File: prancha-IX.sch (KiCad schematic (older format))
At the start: 32 parts

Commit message: conector de 70 pinos para a interconexão das placas e término do desenho da prancha 5.
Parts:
- added P?: CONN_35X2, symbol CONN_35X2
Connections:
- new net ?: P?.1 (P1), P?.10 (P10), P?.11 (P11), P?.12 (P12), P?.13 (P13), P?.14 (P14), P?.15 (P15), P?.16 (P16), P?.17 (P17), P?.18 (P18), P?.19 (P19), P?.2 (P2), P?.20 (P20), P?.21 (P21), P?.22 (P22), P?.23 (P23), P?.24 (P24), P?.25, P?.26 (P26), P?.27 (P27), P?.28 (P28), P?.29 (P29), P?.3 (P3), P?.30 (P30), P?.31 (P31), P?.32 (P32), P?.33 (P33), P?.34 (P34), P?.35 (P35), P?.36 (P36), P?.37 (P37), P?.38 (P38), P?.39 (P39), P?.4 (P4), P?.40 (P40), P?.41 (P41), P?.42 (P42), P?.43 (P43), P?.44 (P44), P?.45 (P45), P?.46 (P46), P?.47 (P47), P?.48 (P48), P?.49 (P49), P?.5 (P5), P?.50 (P50), P?.51 (P51), P?.52 (P52), P?.53 (P53), P?.54 (P54), P?.55 (P55), P?.56 (P56), P?.57 (P57), P?.58 (P58), P?.59 (P59), P?.6 (P6), P?.60 (P60), P?.61 (P61), P?.62 (P62), P?.63 (P63), P?.64 (P64), P?.65 (P65), P?.66 (P66), P?.67 (P67), P?.68 (P68), P?.69 (P69), P?.7 (P7), P?.70 (P70), P?.8 (P8), P?.9 (P9)
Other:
- moved on the sheet: 1A_P9A, 1A_P9B, 1B_P9A, 1B_P9B, 1C_P9A, 1C_P9B, 1D_P9A, 1D_P9B, 1E_P9A, 1E_P9B, 1E_P9C, 1E_P9D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

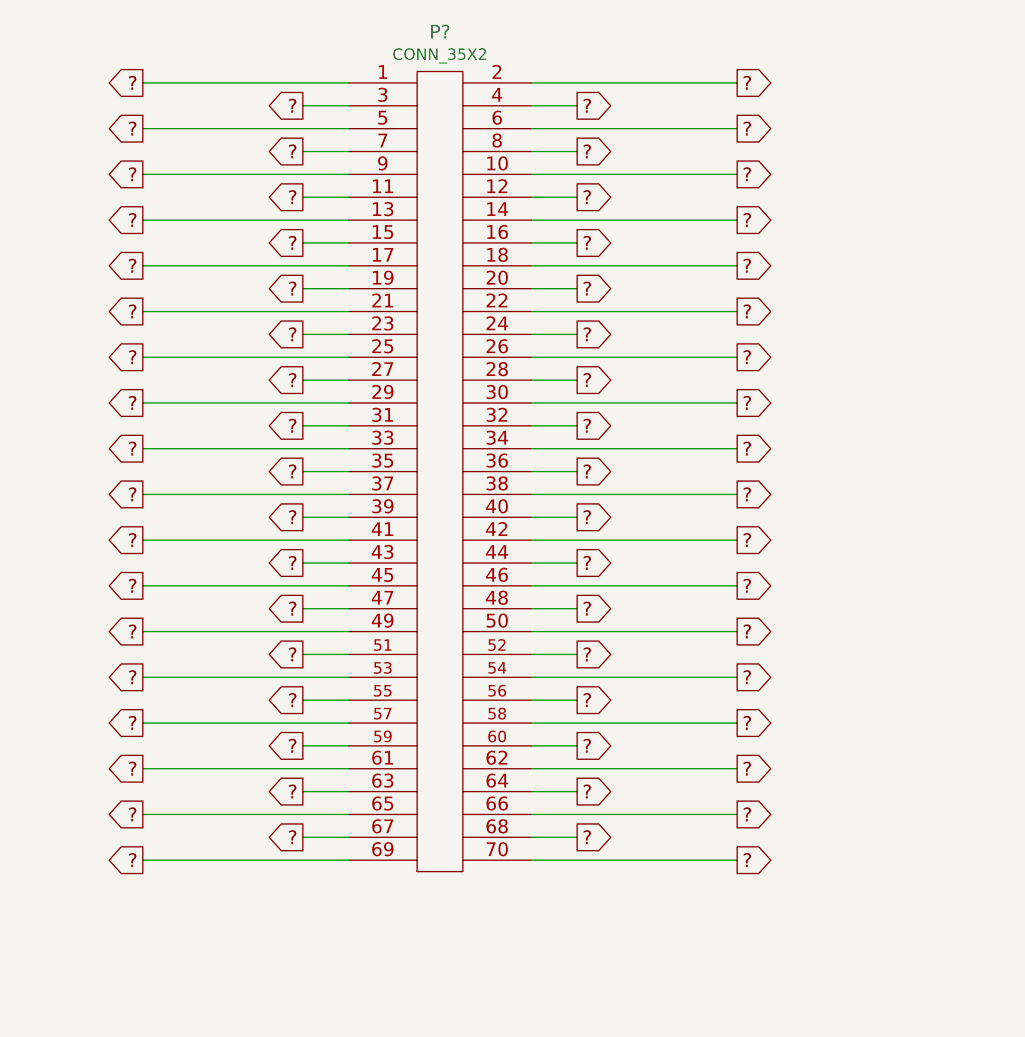
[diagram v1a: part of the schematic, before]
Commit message: sinais do conector da prancha 9
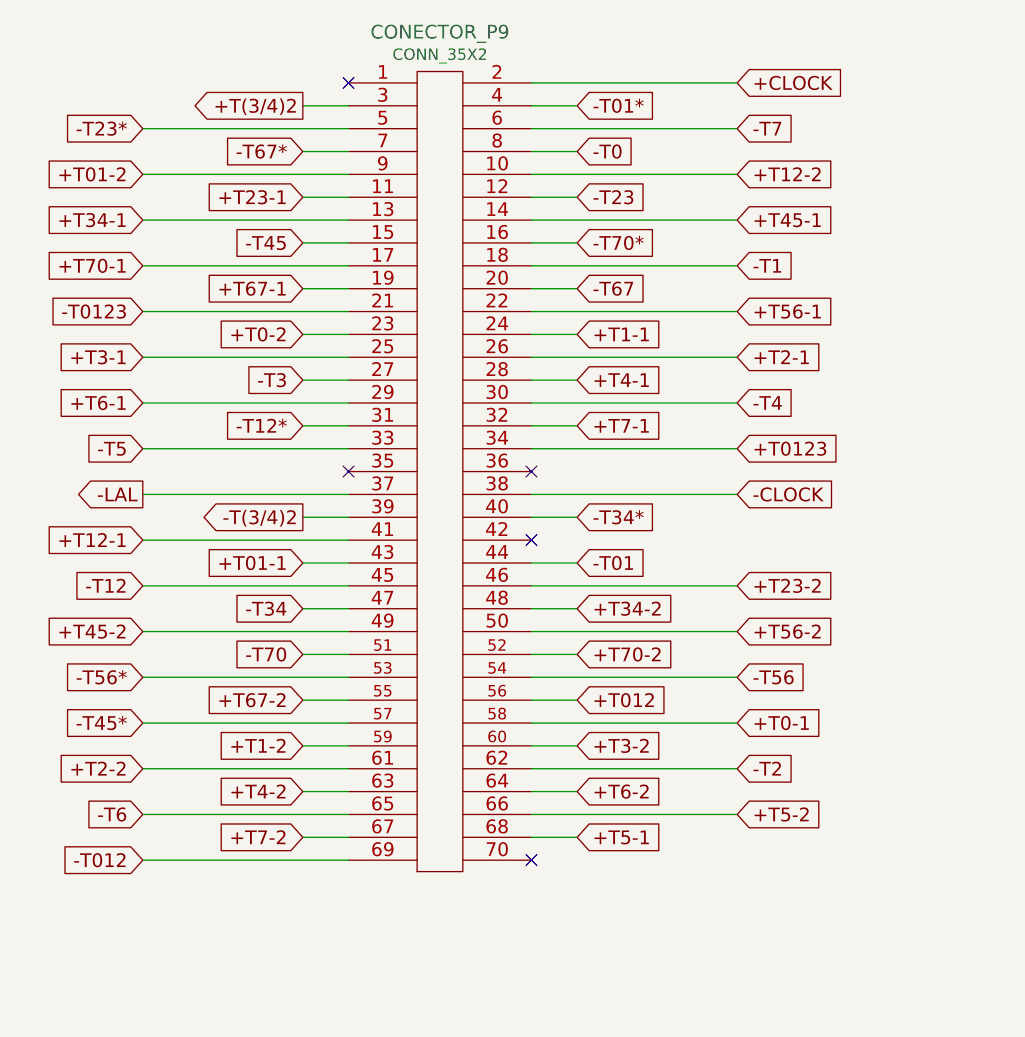
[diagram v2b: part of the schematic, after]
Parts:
- gave numbers to parts that had none: 1
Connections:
- net +CLOCK: now also CONECTOR_P9.2 (P2)
- net +T(3/4)2: now also CONECTOR_P9.3 (P3)
- net +T0-1: now also CONECTOR_P9.58 (P58)
- net +T0-2: now also CONECTOR_P9.23 (P23)
- net +T01-1: now also CONECTOR_P9.43 (P43)
- net +T01-2: now also CONECTOR_P9.9 (P9)
- net +T012: now also CONECTOR_P9.56 (P56)
- net +T0123: now also CONECTOR_P9.34 (P34)
- net +T1-1: now also CONECTOR_P9.24 (P24)
- net +T1-2: now also CONECTOR_P9.59 (P59)
- net +T12-1: now also CONECTOR_P9.41 (P41)
- net +T12-2: now also CONECTOR_P9.10 (P10)
- net +T2-1: now also CONECTOR_P9.26 (P26)
- net +T2-2: now also CONECTOR_P9.61 (P61)
- net +T23-1: now also CONECTOR_P9.11 (P11)
- net +T23-2: now also CONECTOR_P9.46 (P46)
- net +T3-1: now also CONECTOR_P9.25
- net +T3-2: now also CONECTOR_P9.60 (P60)
- net +T34-1: now also CONECTOR_P9.13 (P13)
- net +T34-2: now also CONECTOR_P9.48 (P48)
- net +T4-1: now also CONECTOR_P9.28 (P28)
- net +T4-2: now also CONECTOR_P9.63 (P63)
- net +T45-1: now also CONECTOR_P9.14 (P14)
- net +T45-2: now also CONECTOR_P9.49 (P49)
- net +T5-1: now also CONECTOR_P9.68 (P68)
- net +T5-2: now also CONECTOR_P9.66 (P66)
- net +T56-1: now also CONECTOR_P9.22 (P22)
- net +T56-2: now also CONECTOR_P9.50 (P50)
- net +T6-1: now also CONECTOR_P9.29 (P29)
- net +T6-2: now also CONECTOR_P9.64 (P64)
- net +T67-1: now also CONECTOR_P9.19 (P19)
- net +T67-2: now also CONECTOR_P9.55 (P55)
- net +T7-1: now also CONECTOR_P9.32 (P32)
- net +T7-2: now also CONECTOR_P9.67 (P67)
- net +T70-1: now also CONECTOR_P9.17 (P17)
- net +T70-2: now also CONECTOR_P9.52 (P52)
- net -CLOCK: now also CONECTOR_P9.38 (P38)
- net -LAL: now also CONECTOR_P9.37 (P37)
- net -T(3/4)2: now also CONECTOR_P9.39 (P39)
- net -T0: now also CONECTOR_P9.8 (P8)
- net -T01: now also CONECTOR_P9.44 (P44)
- net -T01*: now also CONECTOR_P9.4 (P4)
- net -T012: now also CONECTOR_P9.69 (P69)
- net -T0123: now also CONECTOR_P9.21 (P21)
- net -T1: now also CONECTOR_P9.18 (P18)
- net -T12: now also CONECTOR_P9.45 (P45)
- net -T12*: now also CONECTOR_P9.31 (P31)
- net -T2: now also CONECTOR_P9.62 (P62)
- net -T23: now also CONECTOR_P9.12 (P12)
- net -T23*: now also CONECTOR_P9.5 (P5)
- net -T3: now also CONECTOR_P9.27 (P27)
- net -T34: now also CONECTOR_P9.47 (P47)
- net -T34*: now also CONECTOR_P9.40 (P40)
- net -T4: now also CONECTOR_P9.30 (P30)
- net -T45: now also CONECTOR_P9.15 (P15)
- net -T45*: now also CONECTOR_P9.57 (P57)
- net -T5: now also CONECTOR_P9.33 (P33)
- net -T56: now also CONECTOR_P9.54 (P54)
- net -T56*: now also CONECTOR_P9.53 (P53)
- net -T6: now also CONECTOR_P9.65 (P65)
- net -T67: now also CONECTOR_P9.20 (P20)
- net -T67*: now also CONECTOR_P9.7 (P7)
- net -T7: now also CONECTOR_P9.6 (P6)
- net -T70: now also CONECTOR_P9.51 (P51)
- net -T70*: now also CONECTOR_P9.16 (P16)
- removed net ?: CONECTOR_P9.1 (P1), CONECTOR_P9.10 (P10), CONECTOR_P9.11 (P11), CONECTOR_P9.12 (P12), CONECTOR_P9.13 (P13), CONECTOR_P9.14 (P14), CONECTOR_P9.15 (P15), CONECTOR_P9.16 (P16), CONECTOR_P9.17 (P17), CONECTOR_P9.18 (P18), CONECTOR_P9.19 (P19), CONECTOR_P9.2 (P2), CONECTOR_P9.20 (P20), CONECTOR_P9.21 (P21), CONECTOR_P9.22 (P22), CONECTOR_P9.23 (P23), CONECTOR_P9.24 (P24), CONECTOR_P9.25, CONECTOR_P9.26 (P26), CONECTOR_P9.27 (P27), CONECTOR_P9.28 (P28), CONECTOR_P9.29 (P29), CONECTOR_P9.3 (P3), CONECTOR_P9.30 (P30), CONECTOR_P9.31 (P31), CONECTOR_P9.32 (P32), CONECTOR_P9.33 (P33), CONECTOR_P9.34 (P34), CONECTOR_P9.35 (P35), CONECTOR_P9.36 (P36), CONECTOR_P9.37 (P37), CONECTOR_P9.38 (P38), CONECTOR_P9.39 (P39), CONECTOR_P9.4 (P4), CONECTOR_P9.40 (P40), CONECTOR_P9.41 (P41), CONECTOR_P9.42 (P42), CONECTOR_P9.43 (P43), CONECTOR_P9.44 (P44), CONECTOR_P9.45 (P45), CONECTOR_P9.46 (P46), CONECTOR_P9.47 (P47), CONECTOR_P9.48 (P48), CONECTOR_P9.49 (P49), CONECTOR_P9.5 (P5), CONECTOR_P9.50 (P50), CONECTOR_P9.51 (P51), CONECTOR_P9.52 (P52), CONECTOR_P9.53 (P53), CONECTOR_P9.54 (P54), CONECTOR_P9.55 (P55), CONECTOR_P9.56 (P56), CONECTOR_P9.57 (P57), CONECTOR_P9.58 (P58), CONECTOR_P9.59 (P59), CONECTOR_P9.6 (P6), CONECTOR_P9.60 (P60), CONECTOR_P9.61 (P61), CONECTOR_P9.62 (P62), CONECTOR_P9.63 (P63), CONECTOR_P9.64 (P64), CONECTOR_P9.65 (P65), CONECTOR_P9.66 (P66), CONECTOR_P9.67 (P67), CONECTOR_P9.68 (P68), CONECTOR_P9.69 (P69), CONECTOR_P9.7 (P7), CONECTOR_P9.70 (P70), CONECTOR_P9.8 (P8), CONECTOR_P9.9 (P9)
- no-connect marks 0 -> 5

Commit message: numerando todas referencias e corrigindo erros de referencias duplas ou pacotes inconsistentes
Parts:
- C1_P9: renamed from C?; value C -> 1K8
- C2_P9, C3_P9: renamed from C?; value 60pF -> 68pF
- C4_P9: renamed from C?; value C -> 680pF
- C5_P9: renamed from C?; value C -> 0,01uF
- L1_P9: renamed from L?; value INDUCTOR -> 30uH
- Q1_P9, Q2_P9, Q3_P9: renamed from Q?; value BC185 -> BF185
- R1_P9: renamed from R?; value R -> 390R
- gave numbers to parts that had none: 6
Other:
- moved on the sheet: C1_P9, C2_P9, C3_P9, C4_P9, C5_P9, L1_P9, Q1_P9, Q2_P9, Q3_P9, R1_P9, R2_P9, R3_P9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

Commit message: wip. acho que preciso separar cada uma das pranchas em um projeto de PCB independente.
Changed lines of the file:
@@
 	22250 13700 22250 13550
 Wire Wire Line
-	22950 13550 22250 13550
+	22250 13550 22950 13550
 Wire Wire Line
 	22950 12450 22950 14800
